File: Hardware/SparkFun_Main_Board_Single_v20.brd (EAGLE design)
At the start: 86.4 x 73.7 mm, 128 parts, among them J1 MICROMOD-2222-C, J10 MICRO-SD-PUSH-PUSH-EXT-PIN, J2 Vertical Qwiic Connector, J4 QWIIC_RIGHT_ANGLE, J5 CORTEX_JTAG_DEBUG_MINIMUM_PTH, J6 MICROMOD_FUNCTION_MAIN, Q1 3.1A/30V/105mΩ, Q2 20V/4.2A/52mΩ/1.4W, U1 STG3856QTR, U2 MCP73831, U3 ESD Diode, U4 AP7347DQ-33W5-7K-3.3V, U5 AP7361C-33

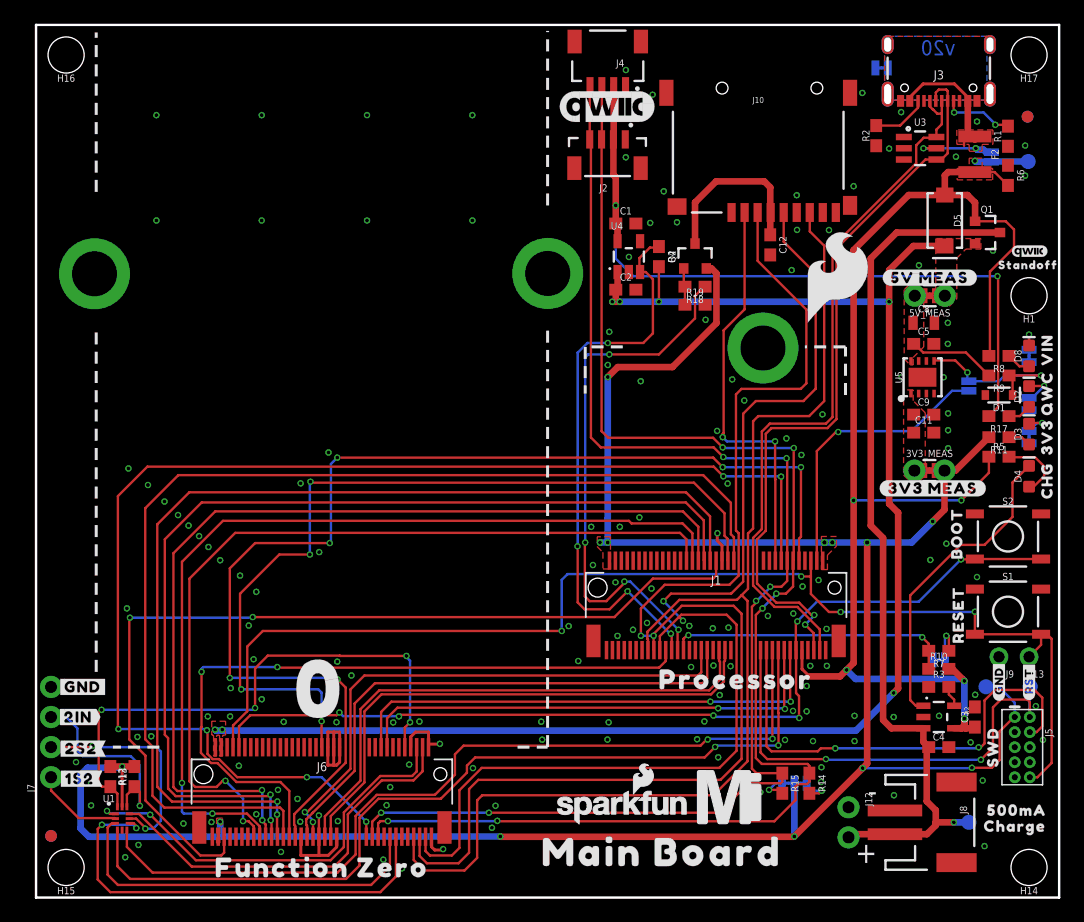
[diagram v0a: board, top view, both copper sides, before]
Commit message: Fixes measure pth alignment
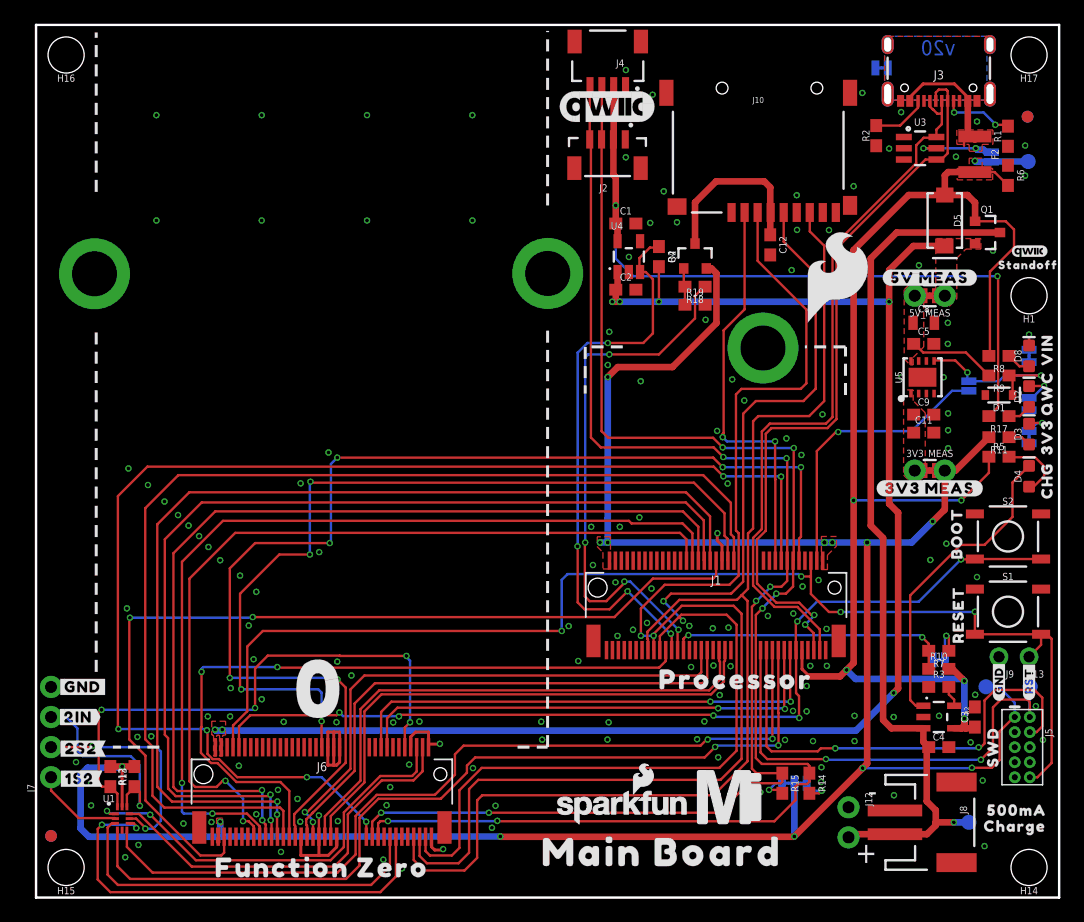
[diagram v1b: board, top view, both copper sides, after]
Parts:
- moved U$52 1.28 mm to (71.6, 19.9)
- moved U$26 0.25 mm to (75.4, 34.5)
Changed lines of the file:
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@@
 <attribute name="VALUE" x="77.851" y="62.738" size="0.6096" layer="27" font="vector" ratio="20" rot="R270" align="top-center"/>
 </element>
-<element name="3V3_MEAS" library="SparkFun-Jumpers" package="COMBO-JUMPER_2_NC_TRACE" value="JUMPER-COMBO_2_NC_TRACE" x="75.4126" y="36.0426" smashed="yes">
-<attribute name="NAME" x="75.4126" y="37.1856" size="0.6096" layer="25" font="vector" ratio="20" align="bottom-center"/>
-<attribute name="VALUE" x="75.4126" y="34.8996" size="0.6096" layer="27" font="vector" ratio="20" align="top-center"/>
+<element name="3V3_MEAS" library="SparkFun-Jumpers" package="COMBO-JUMPER_2_NC_TRACE" value="JUMPER-COMBO_2_NC_TRACE" x="75.438" y="36.0426" smashed="yes">
+<attribute name="NAME" x="75.438" y="37.1856" size="0.6096" layer="25" font="vector" ratio="20" align="bottom-center"/>
+<attribute name="VALUE" x="75.438" y="34.8996" size="0.6096" layer="27" font="vector" ratio="20" align="top-center"/>
 </element>
 <element name="R9" library="SparkFun-Resistors" package="0603" value="100k" x="81.28" y="44.069" smashed="yes" rot="R180">
@@
 <attribute name="VALUE" x="51.816" y="54.102" size="0.6096" layer="27" font="vector" ratio="20" rot="R270" align="top-center"/>
 </element>
-<element name="U$26" library="top" package="#3V3_MEAS#6522" value="" x="75.692" y="34.544" smashed="yes"/>
+<element name="U$26" library="top" package="#3V3_MEAS#6522" value="" x="75.438" y="34.544" smashed="yes"/>
 <element name="U$31" library="top" package="#5V_MEAS#6522" value="" x="75.438" y="52.324" smashed="yes"/>
 <element name="U$33" library="top" package="500MA6520" value="" x="82.804" y="7.366" smashed="yes"/>
@@
 <element name="U$50" library="top" package="#3V3_LED#22" value="" x="79.375" y="38.862" smashed="yes" rot="MR0"/>
 <element name="U$51" library="top" package="#QWIIC_LED#22" value="" x="78.613" y="41.275" smashed="yes" rot="MR0"/>
-<element name="U$52" library="top" package="#DIVIDER#23" value="" x="70.358" y="20.066" smashed="yes" rot="MR0"/>
+<element name="U$52" library="top" package="#DIVIDER#23" value="" x="71.628" y="19.939" smashed="yes" rot="MR0"/>
 <element name="U$53" library="top" package="#VIN_LED#24" value="" x="79.502" y="45.847" smashed="yes" rot="MR0"/>
 <element name="U$30" library="top" package="#I2C#501" value="" x="64.008" y="11.43" smashed="yes" rot="MR0"/>
@@
 <wire x1="7.2698" y1="11.0608" x2="6.2738" y2="11.0608" width="0.5588" layer="1"/>
 <wire x1="7.2698" y1="11.0608" x2="8.3058" y2="11.0608" width="0.5588" layer="1"/>
-<wire x1="76.6826" y1="36.0426" x2="76.6826" y2="32.7406" width="0.5588" layer="1"/>
-<wire x1="76.6826" y1="32.7406" x2="75.692" y2="31.75" width="0.5588" layer="1"/>
+<wire x1="76.6826" y1="32.7406" x2="76.581" y2="32.639" width="0.5588" layer="1"/>
+<wire x1="76.708" y1="32.766" x2="76.6826" y2="32.7406" width="0.5588" layer="1"/>
+<wire x1="76.581" y1="32.639" x2="75.692" y2="31.75" width="0.5588" layer="1"/>
 <wire x1="39.2176" y1="5.1308" x2="39.1922" y2="5.1562" width="0.5588" layer="1"/>
 <contactref element="I2C_PU" pad="2"/>
@@
 <via x="64.008" y="5.1562" extent="1-16" drill="0.3048"/>
 <wire x1="7.2698" y1="7.6648" x2="7.2698" y2="11.0608" width="0.254" layer="1"/>
-<wire x1="75.9206" y1="36.0426" x2="76.6826" y2="36.0426" width="0.5588" layer="1"/>
+<wire x1="75.946" y1="36.0426" x2="76.708" y2="36.0426" width="0.5588" layer="1"/>
 <wire x1="48.26" y1="29.972" x2="66.548" y2="29.972" width="0.5588" layer="16"/>
 <wire x1="15.5448" y1="5.207" x2="15.4686" y2="5.1308" width="0.5588" layer="16"/>
-<wire x1="15.4686" y1="5.1308" x2="11.43" y2="5.1308" width="0.5588" layer="16"/>
-<wire x1="11.43" y1="5.1308" x2="4.4704" y2="5.1308" width="0.5588" layer="16"/>
+<wire x1="15.4686" y1="5.1308" x2="4.4704" y2="5.1308" width="0.5588" layer="16"/>
 <wire x1="3.7592" y1="5.842" x2="3.7592" y2="10.3632" width="0.5588" layer="16"/>
 <wire x1="3.7592" y1="10.3632" x2="4.3552" y2="10.9592" width="0.5588" layer="16"/>
@@
 <wire x1="78.9596" y1="10.922" x2="69.7738" y2="10.922" width="0.2032" layer="16"/>
 <wire x1="80.43" y1="38.862" x2="77.6106" y2="36.0426" width="0.5588" layer="1"/>
-<wire x1="77.6106" y1="36.0426" x2="76.6826" y2="36.0426" width="0.5588" layer="1"/>
+<wire x1="77.6106" y1="36.0426" x2="76.708" y2="36.0426" width="0.5588" layer="1"/>
 <wire x1="69.723" y1="10.922" x2="69.7738" y2="10.922" width="0.5588" layer="1"/>
 <wire x1="64.008" y1="5.1562" x2="63.9826" y2="5.1308" width="0.5588" layer="1"/>
@@
 <wire x1="57.4324" y1="48.4888" x2="57.4324" y2="52.6875375" width="0.5588" layer="1"/>
 <wire x1="53.721" y1="44.7774" x2="57.4324" y2="48.4888" width="0.5588" layer="1"/>
+<wire x1="76.708" y1="32.766" x2="76.708" y2="36.0426" width="0.5588" layer="1"/>
 </signal>
 <signal name="3.3V_EN">

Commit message: Remakes production files
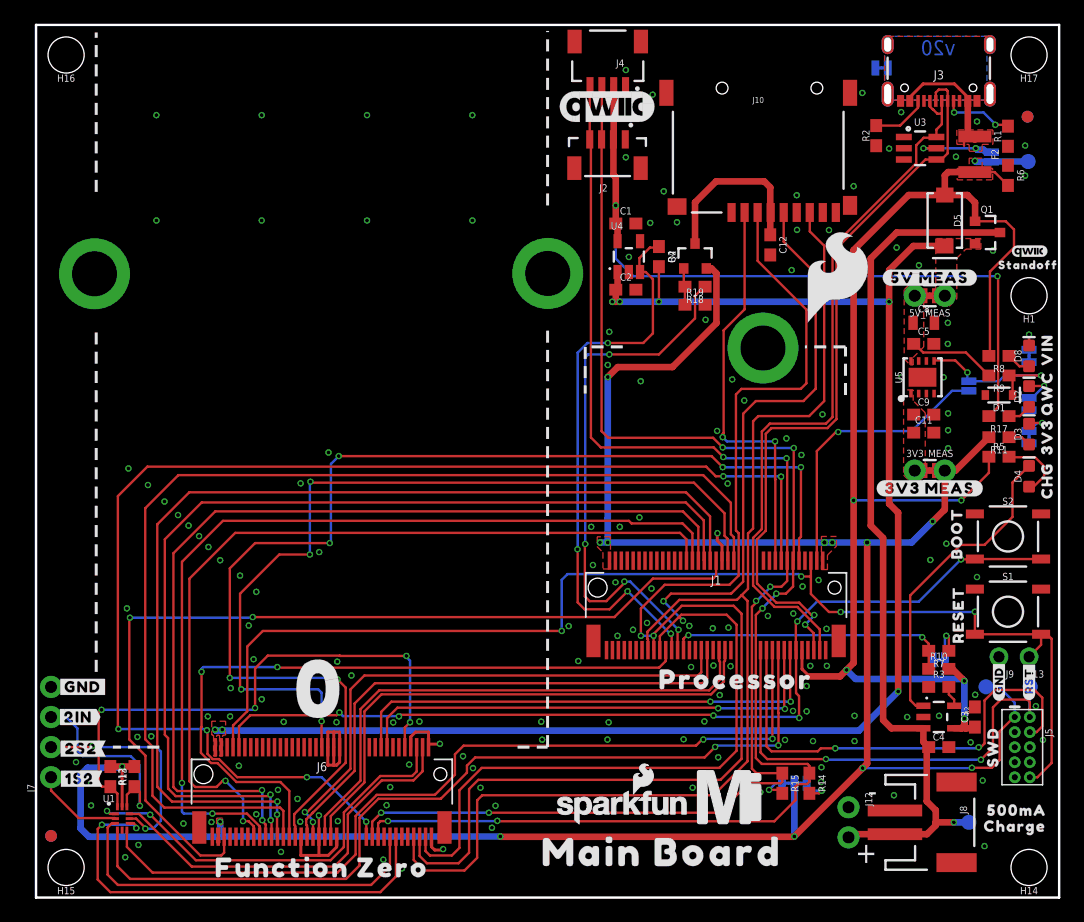
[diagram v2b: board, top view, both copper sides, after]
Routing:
- net GND: vias 157 -> 161

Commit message: Updates silk on multiplexing PTH
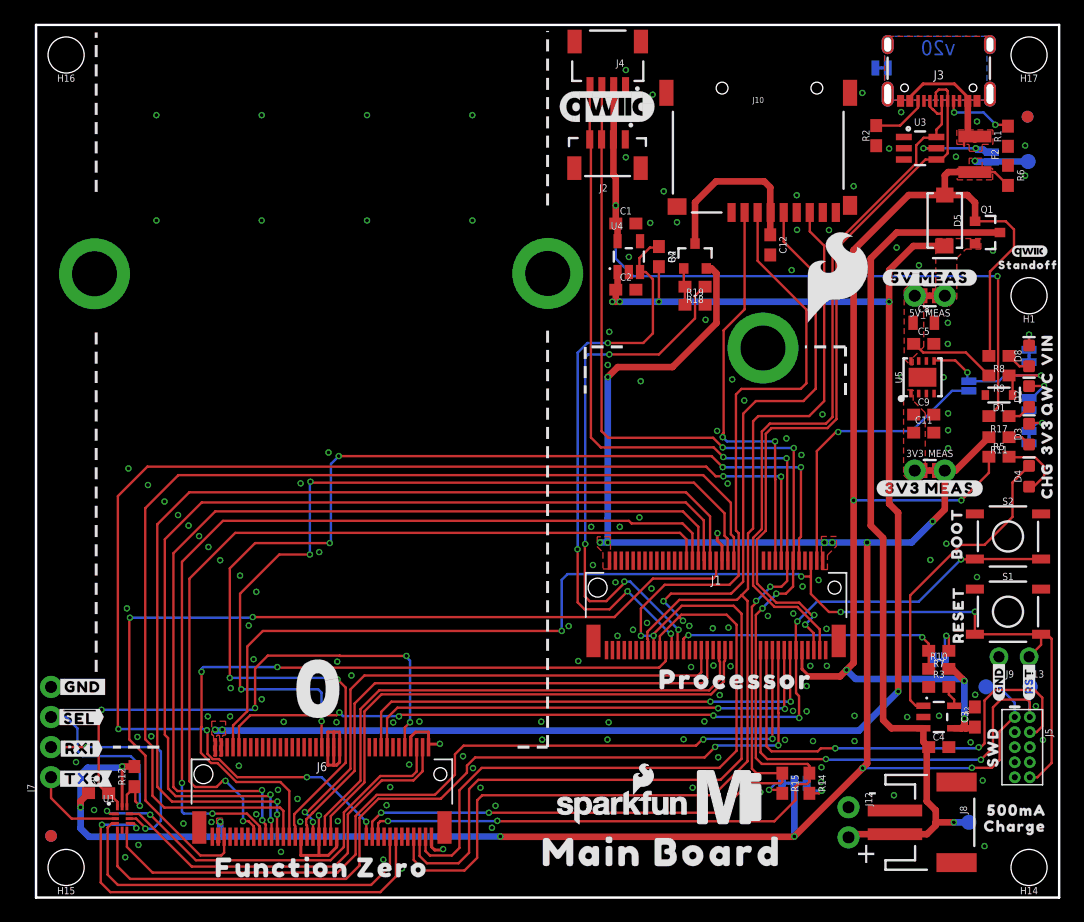
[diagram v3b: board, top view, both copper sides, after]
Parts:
- U$1: device top:#1S2#3 -> top:#TXO#7
- U$12: device top:#2IN#0 -> top:##SEL##5
- U$19: device bot:#1S2#3 -> bot:##SEL##3
- U$2: device top:#2S2#3 -> top:#RXI#6
- U$20: device bot:#2IN#0 -> bot:#RXI#4
- U$28: device bot:#2S2#3 -> bot:#TXO#5
- moved U$19 5.21 mm to (3.68, 15.2)
- moved U$20 2.67 mm to (3.68, 12.6)
- moved U$28 2.55 mm to (4.06, 10.0)
- moved R13 1.71 mm to (5.28, 8.81), turned to 0 degrees
- moved U$1 0.38 mm to (4.06, 10.0)
- moved U$2 0.13 mm to (3.68, 12.6)
- moved U$12 0.13 mm to (3.68, 15.2)
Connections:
- net 1S2_MULTIPLEXER renamed TX1/1S2
- net 2IN_MULTIPLEXER renamed !SEL!/2IN
- net 2S2_MULTIPLEXER renamed RX1/2S2
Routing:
- net 3.3V: track 197.1 -> 197.6 mm, vias 13 -> 14
- net GND: vias 161 -> 160
